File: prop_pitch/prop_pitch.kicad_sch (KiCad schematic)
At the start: 54 parts, among them J1 AVR-ISP-6, J2 LOAD1, J3 LOAD2, J4 SERVO1, J6 SERVO2, Q1 MMS8550, U1 ATmega328P-A, U1 TPS563208DDCR, U3 HC-05, U5 AZ1117-5.0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

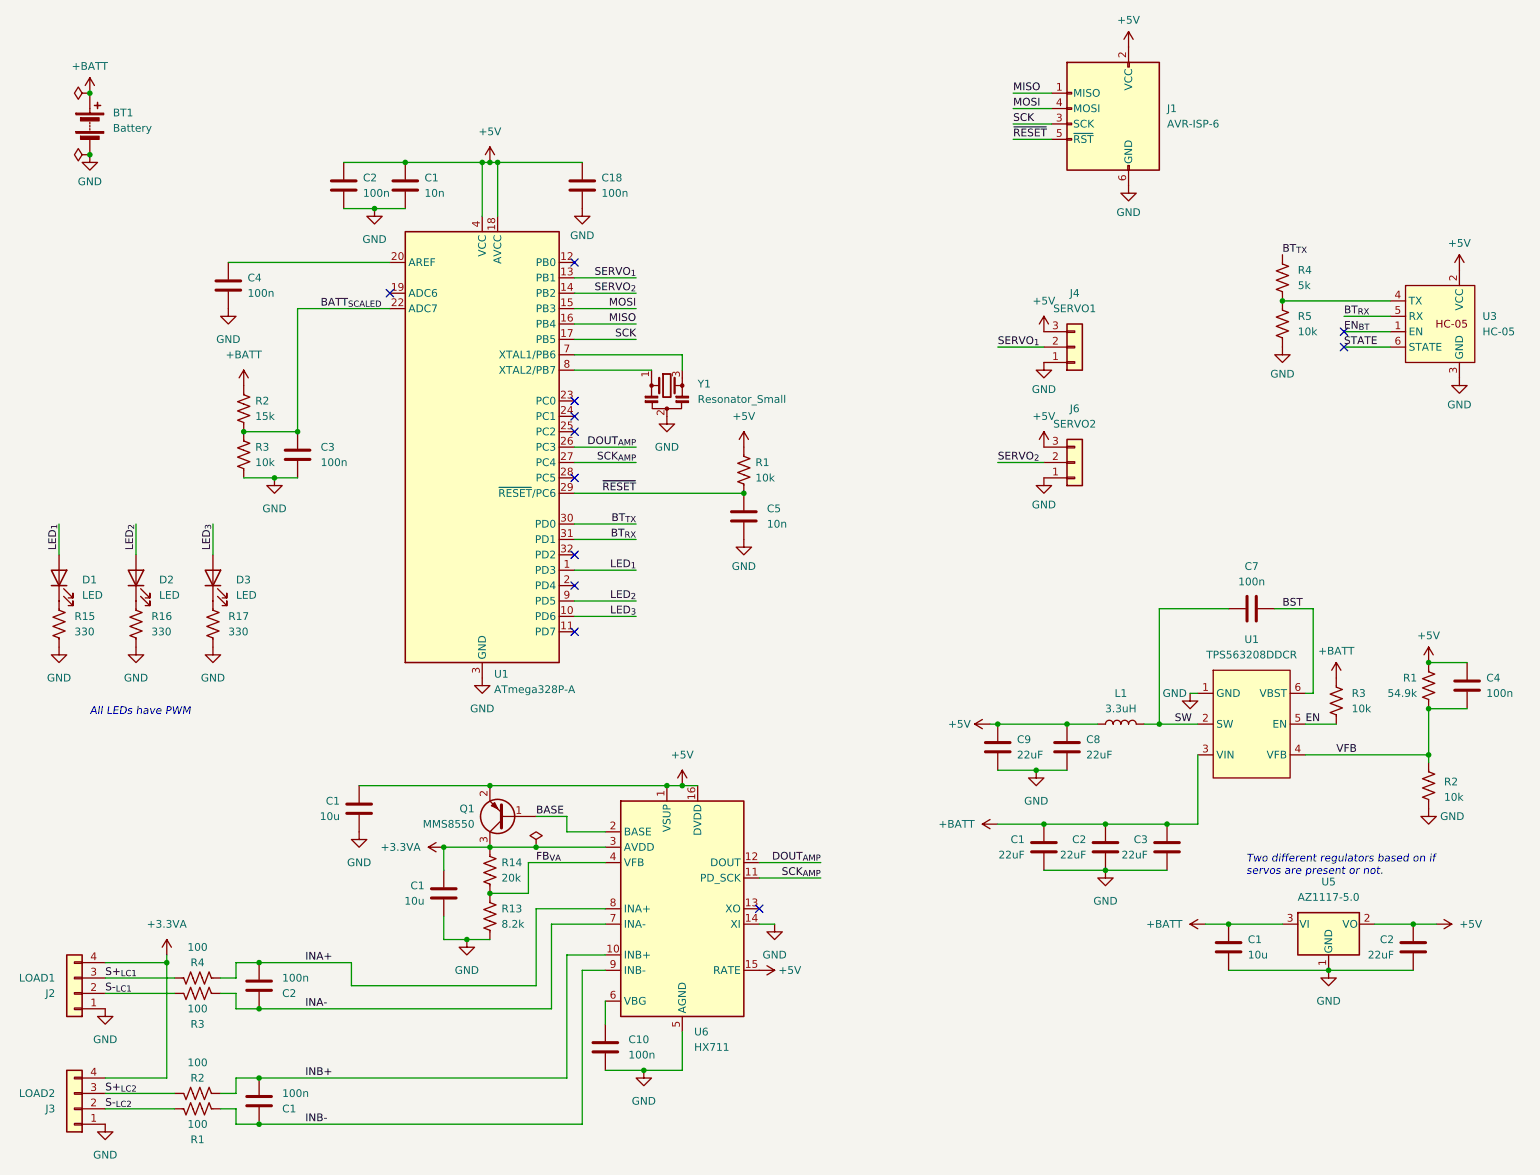
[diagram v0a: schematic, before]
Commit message: Updated spar sensor to reflect order
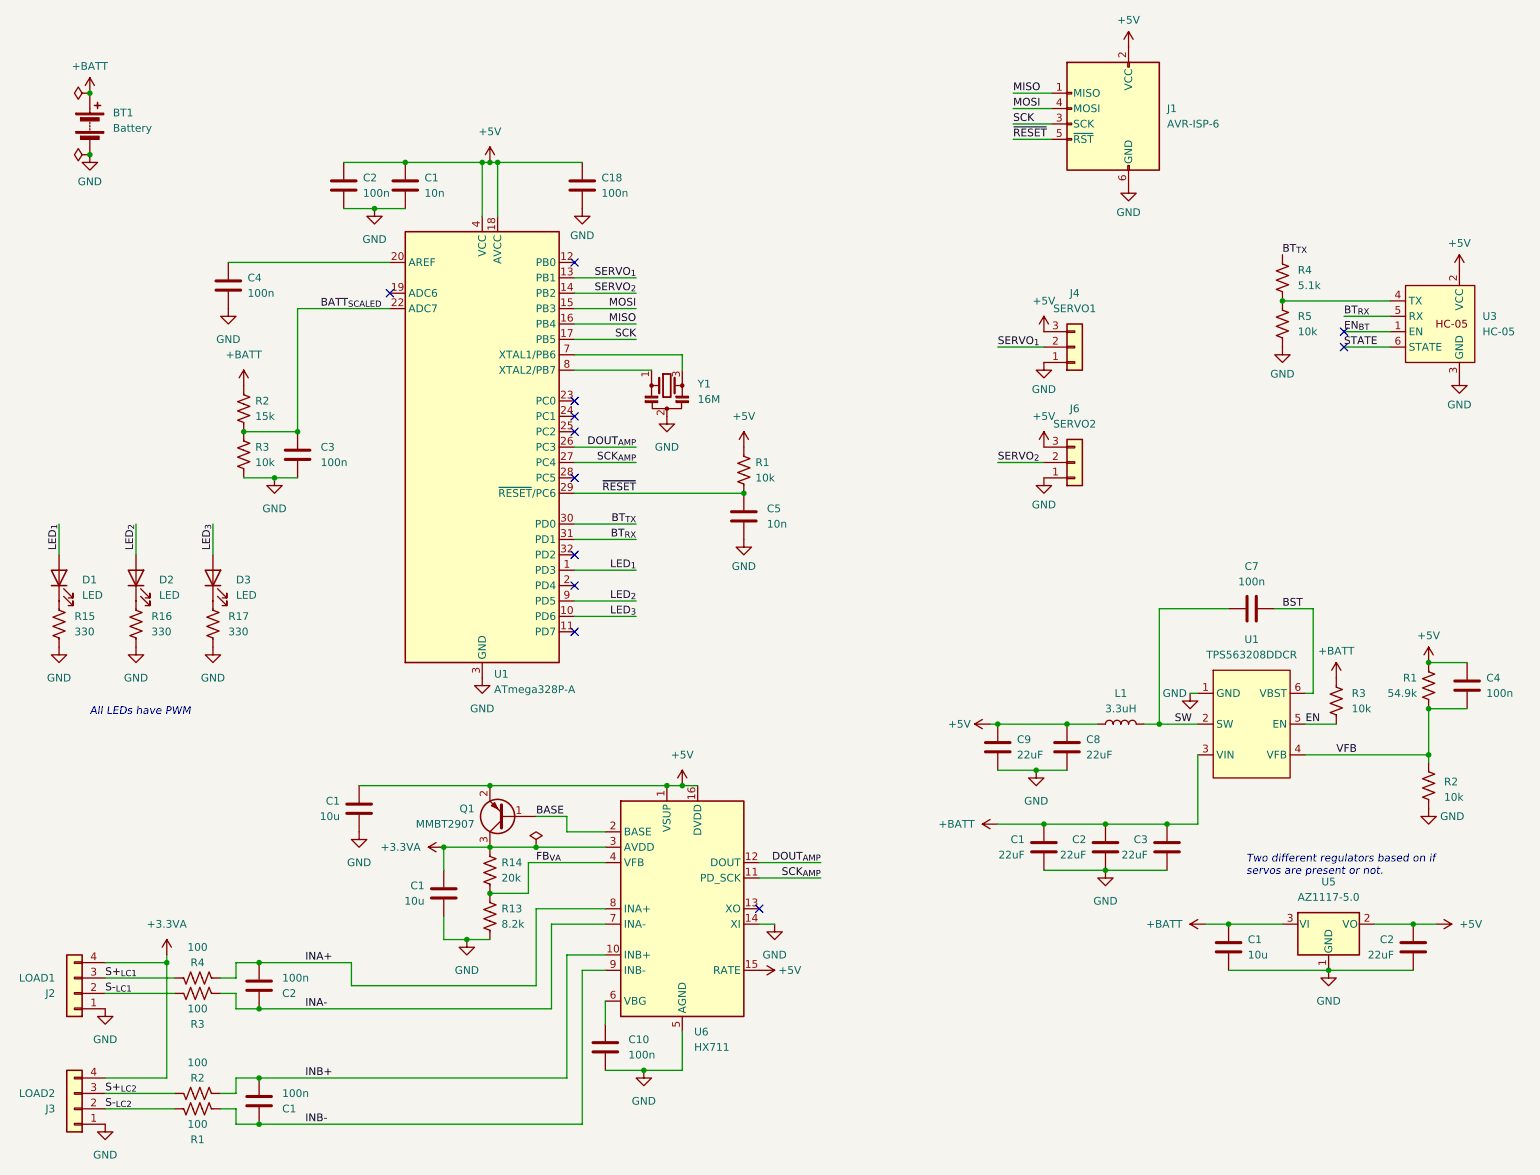
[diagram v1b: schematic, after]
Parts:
- Q1: value MMS8550 -> MMBT2907
- R4: value 5k -> 5.1k
- Y1: value Resonator_Small -> 16M
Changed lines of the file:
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@@
       (effects (font (size 1.27 1.27)) (justify left))
     )
-    (property "Value" "MMS8550" (at 92.71 147.32 0)
+    (property "Value" "MMBT2907" (at 92.71 147.32 0)
       (effects (font (size 1.27 1.27)) (justify left))
     )
@@
       (effects (font (size 1.27 1.27)) hide)
     )
-    (property "Datasheet" "~" (at 97.79 146.05 0)
+    (property "Datasheet" "https://www.mouser.ca/datasheet/2/258/MMBT2907A_SOT_23_-2510709.pdf" (at 97.79 146.05 0)
       (effects (font (size 1.27 1.27)) hide)
     )
@@
       (effects (font (size 1.27 1.27)) (justify left))
     )
-    (property "Value" "5k" (at 228.6 58.42 0)
+    (property "Value" "5.1k" (at 228.6 58.42 0)
       (effects (font (size 1.27 1.27)) (justify left))
     )
@@
       (effects (font (size 1.27 1.27)) (justify left))
     )
-    (property "Value" "Resonator_Small" (at 129.54 77.2033 0)
-      (effects (font (size 1.27 1.27)) (justify left))
-    )
+    (property "Value" "16M" (at 129.54 77.2033 0)
+      (effects (font (size 1.27 1.27)) (justify left))
+    )

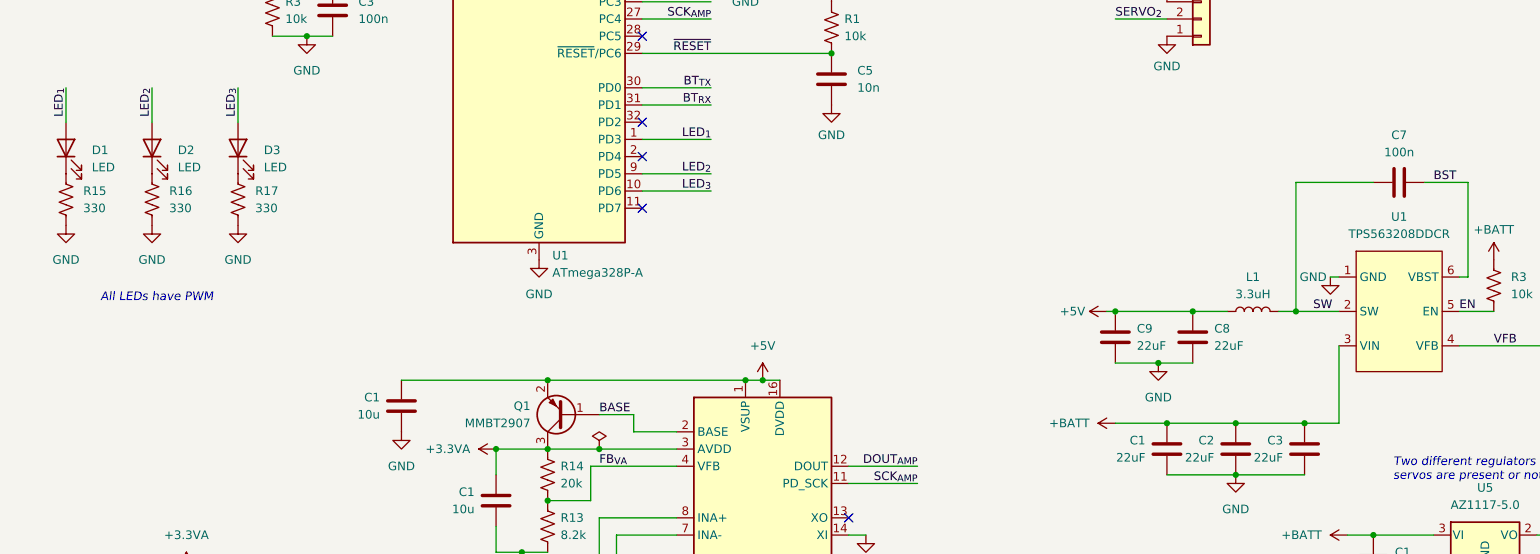
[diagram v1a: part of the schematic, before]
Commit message: Updated for prop pitch order
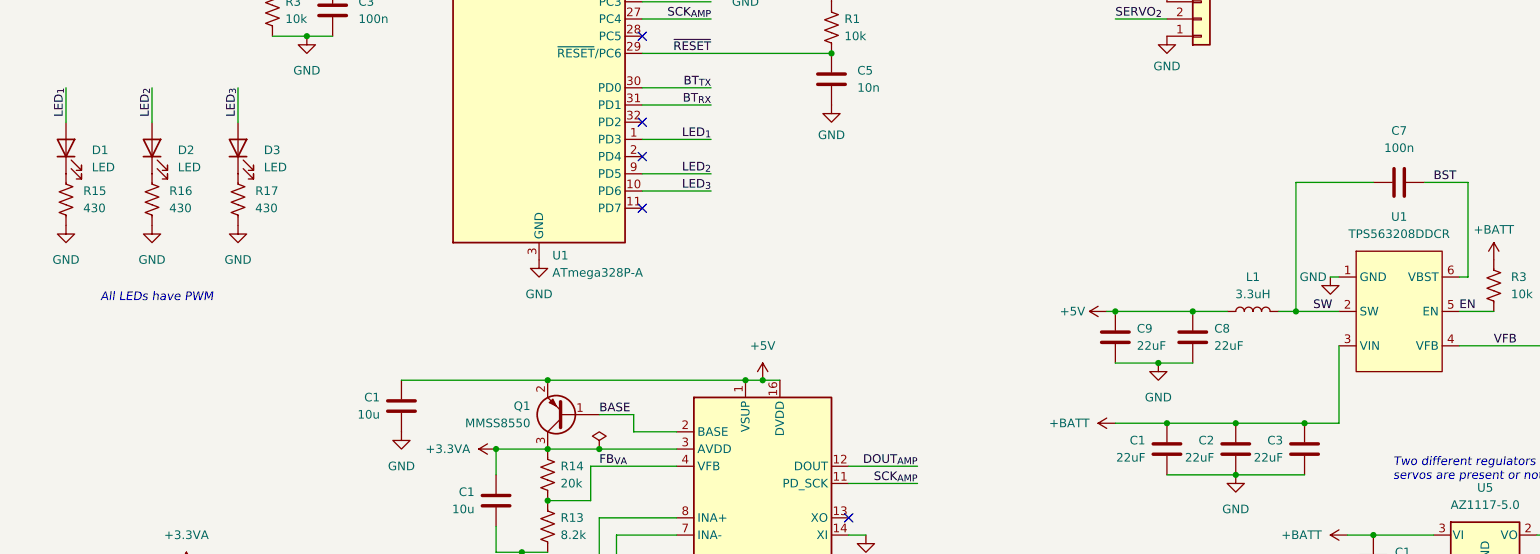
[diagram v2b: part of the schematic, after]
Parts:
- BT1, J2, J3: now left out of the parts list
- Q1: value MMBT2907 -> MMSS8550
- R15, R16, R17: value 330 -> 430
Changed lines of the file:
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@@
       (effects (font (size 1.27 1.27)) (justify left))
     )
-    (property "Value" "330" (at 26.67 115.57 0)
+    (property "Value" "430" (at 26.67 115.57 0)
       (effects (font (size 1.27 1.27)) (justify left))
     )
@@
   )
   (symbol (lib_id "Device:Battery") (at 29.21 31.75 0) (unit 1)
-    (in_bom yes) (on_board yes) (dnp no) (fields_autoplaced)
+    (in_bom no) (on_board yes) (dnp no) (fields_autoplaced)
     (property "Reference" "BT1" (at 33.02 29.9085 0)
       (effects (font (size 1.27 1.27)) (justify left))
@@
   )
   (symbol (lib_id "Connector_Generic:Conn_01x04") (at 26.67 175.26 180) (unit 1)
-    (in_bom yes) (on_board yes) (dnp no)
+    (in_bom no) (on_board yes) (dnp no)
     (property "Reference" "J2" (at 23.495 175.26 0)
       (effects (font (size 1.27 1.27)) (justify left))
@@
       (effects (font (size 1.27 1.27)) (justify left))
     )
-    (property "Value" "330" (at 39.37 115.57 0)
+    (property "Value" "430" (at 39.37 115.57 0)
       (effects (font (size 1.27 1.27)) (justify left))
     )
@@
       (effects (font (size 1.27 1.27)) (justify left))
     )
-    (property "Value" "MMBT2907" (at 92.71 147.32 0)
+    (property "Value" "MMSS8550" (at 92.71 147.32 0)
       (effects (font (size 1.27 1.27)) (justify left))
     )
@@
       (effects (font (size 1.27 1.27)) hide)
     )
-    (property "Datasheet" "https://www.mouser.ca/datasheet/2/258/MMBT2907A_SOT_23_-2510709.pdf" (at 97.79 146.05 0)
+    (property "Datasheet" "`" (at 97.79 146.05 0)
       (effects (font (size 1.27 1.27)) hide)
     )
@@
   (symbol (lib_id "Device:C") (at 220.98 111.76 90) (unit 1)
     (in_bom yes) (on_board yes) (dnp no) (fields_autoplaced)
-    (property "Reference" "C7" (at 220.98 104.775 90)
-      (effects (font (size 1.27 1.27)))
-    )
-    (property "Value" "100n" (at 220.98 107.315 90)
+    (property "Reference" "C7" (at 220.98 104.14 90)
+      (effects (font (size 1.27 1.27)))
+    )
+    (property "Value" "100n" (at 220.98 106.68 90)
       (effects (font (size 1.27 1.27)))
     )
@@
   )
   (symbol (lib_id "Connector_Generic:Conn_01x04") (at 26.67 194.31 180) (unit 1)
-    (in_bom yes) (on_board yes) (dnp no)
+    (in_bom no) (on_board yes) (dnp no)
     (property "Reference" "J3" (at 23.495 194.31 0)
       (effects (font (size 1.27 1.27)) (justify left))
@@
       (effects (font (size 1.27 1.27)) (justify left))
     )
-    (property "Value" "330" (at 52.07 115.57 0)
-      (effects (font (size 1.27 1.27)) (justify left))
-    )
+    (property "Value" "430" (at 52.07 115.57 0)
+      (effects (font (size 1.27 1.27)) (justify left))
+    )
